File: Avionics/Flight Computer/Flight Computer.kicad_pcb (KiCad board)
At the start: 4 copper layers, 50 x 40 mm, 193 parts, among them J1 ERF8-040-05.0-S-DV-K, J2 ERF8-040-05.0-S-DV-K, J3 473460001, J4 734120110, J5 734120110, J6 734120110, U1 CC1310F128RGZR, U12 ATSAME70Q21A-AN, U2 CC1190RGVR, U3 CC2650F128RGZR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

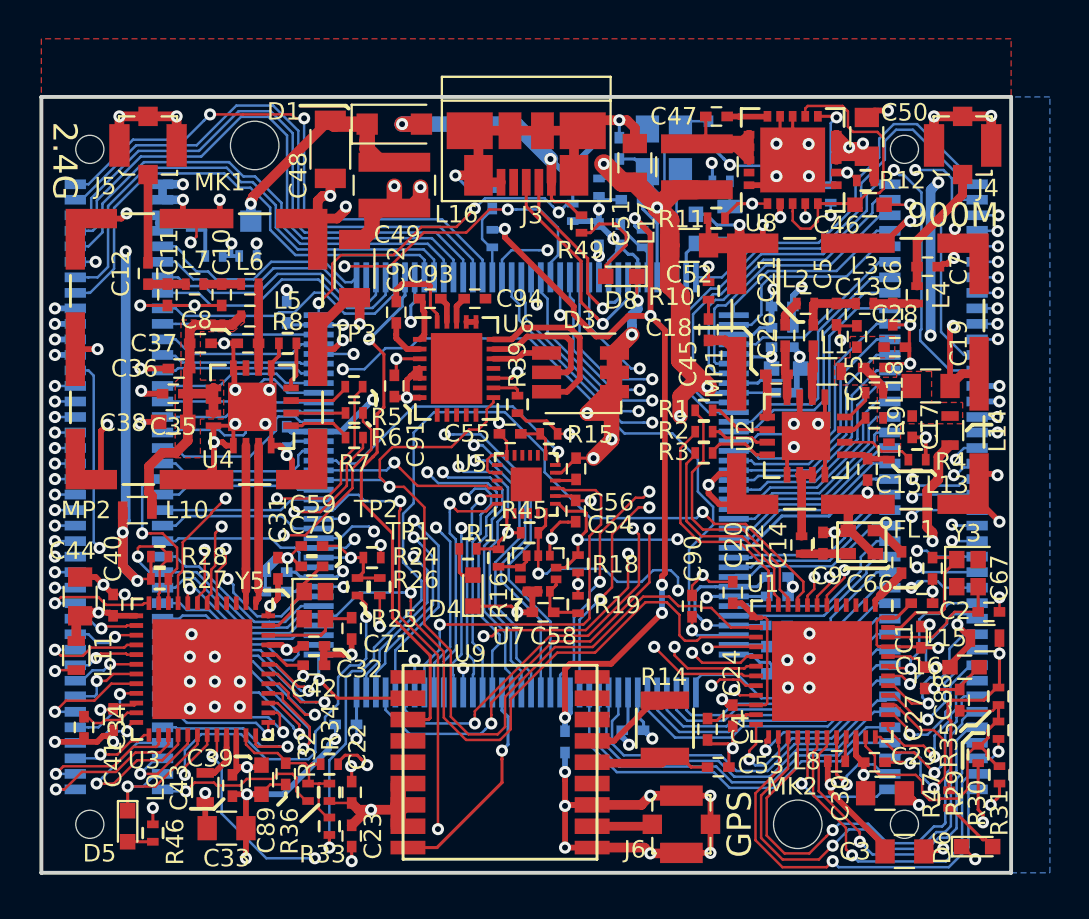
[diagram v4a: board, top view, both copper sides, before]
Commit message: Added Logo, connected GPS SDA/SCL, and cleaned silk.
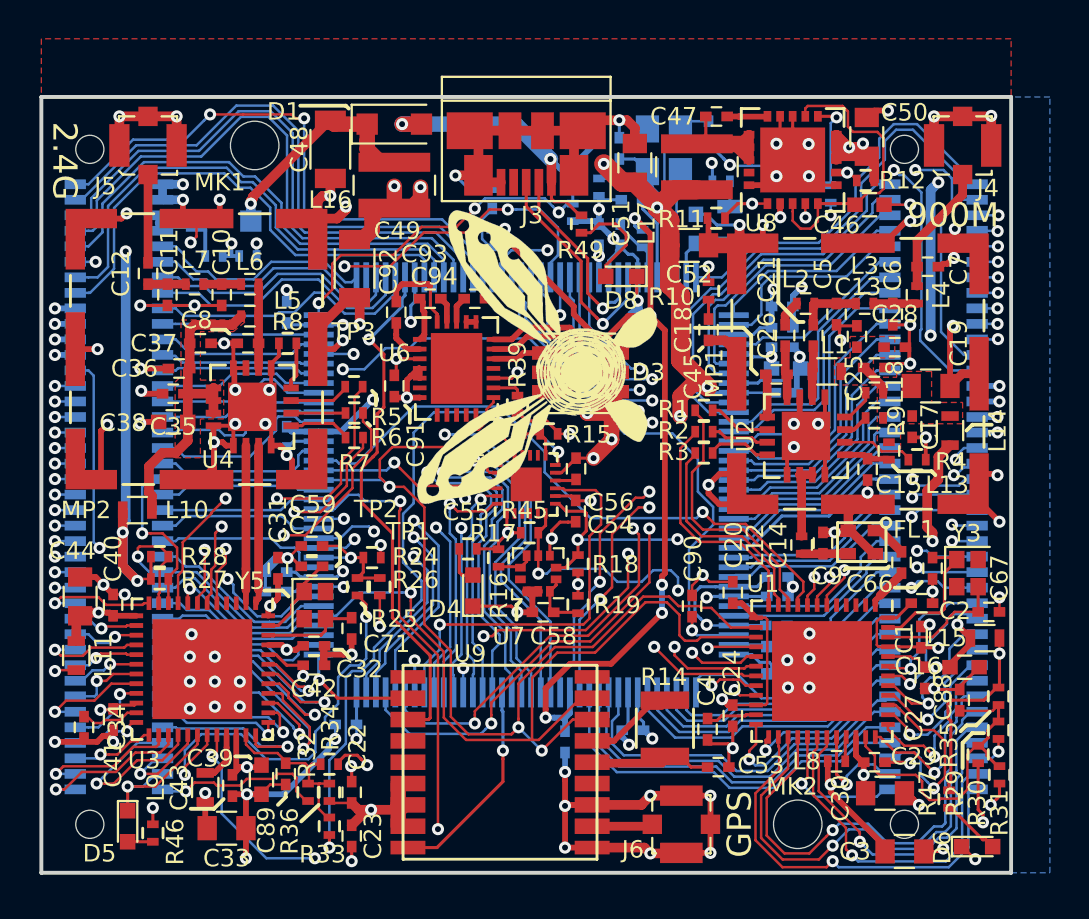
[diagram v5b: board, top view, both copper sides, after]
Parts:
- added G***: LOGO, Symbols:NaviLOGO, F.Cu at (76.2, 99.4)
- added G***: LOGO, Symbols:NaviLOGO, B.Cu at (63.2, 119.0)
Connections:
- U9 pad 16: Net-(U9-Pad16) -> /CPU-SDA
- U9 pad 17: Net-(U9-Pad17) -> /CPU-SCK
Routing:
- net /CPU-SDA: track 64.2 -> 69.6 mm, vias 2 -> 4
- net /CPU-SCK: track 66.5 -> 71.4 mm
- net Net-(C57-Pad1): track 101.4 -> 102.5 mm
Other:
- board text added: "Navi"
- board text added: "Rev 1"

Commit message: Added option resistors for IMU to be connected to radio chips via I2C
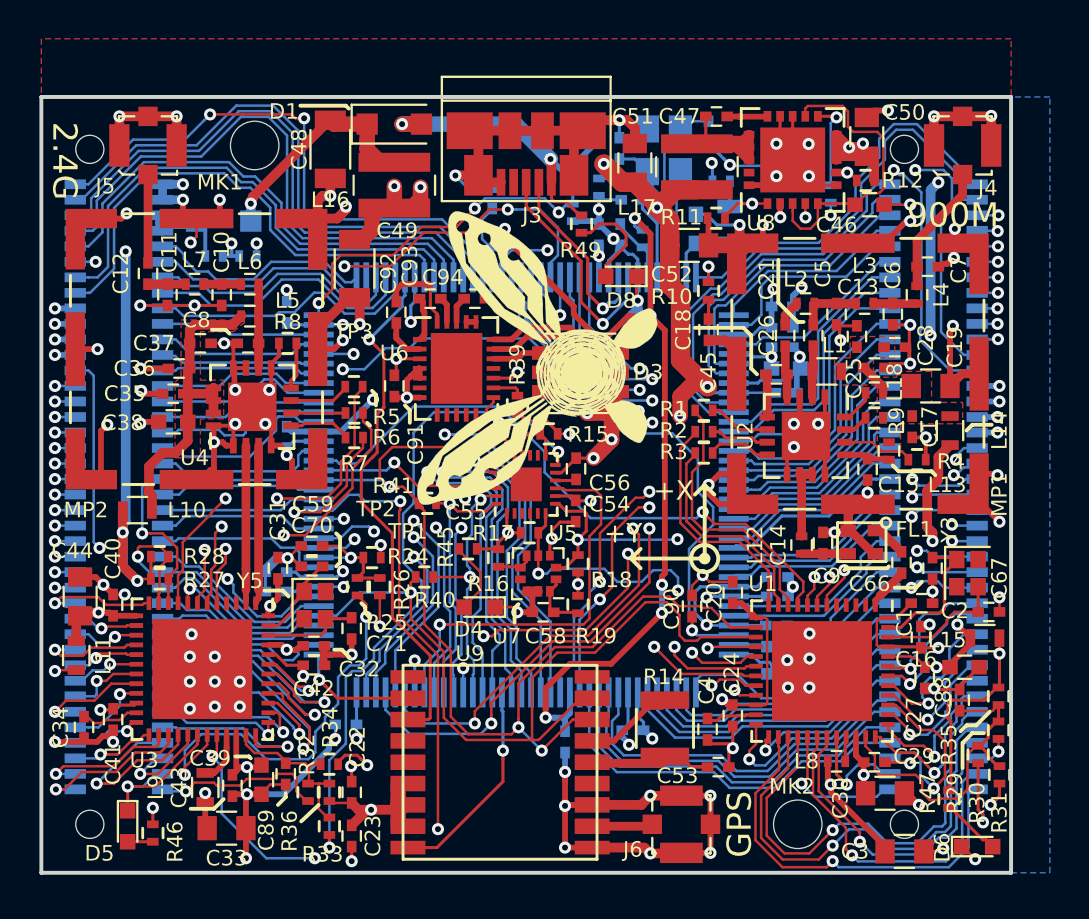
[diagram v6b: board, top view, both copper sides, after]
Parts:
- removed G*** (x2): LOGO, Symbols:NaviLOGO
- added R40: DNP, Resistors_SMD:R_0402, F.Cu at (69.8, 109.8)
- added R41: DNP, Resistors_SMD:R_0402, F.Cu at (69.9, 106.0)
- added U10: Logo, Symbols:NaviLOGO, B.Cu at (63.1, 119.0)
- added U11: Logo, Symbols:NaviLOGO, F.Cu at (76.2, 99.5)
- moved D4 0.92 mm to (72.6, 111.3), turned to 180 degrees
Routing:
- net Net-(D4-Pad2): track 1.97 -> 4.15 mm
- net /GNC_Processor/IMU-SPI-CLK: track 11.3 -> 13.4 mm, vias 1 -> 2
- net GND: track 322.9 -> 321.7 mm
- net /CPU-SCK: track 71.4 -> 72.3 mm
- net Net-(C57-Pad1): track 102.5 -> 101.7 mm
- net /GNC_Processor/IMU-SPI-MOSI: track 12.9 -> 13.6 mm
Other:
- board text added: "+X"
- board text added: "+Y"

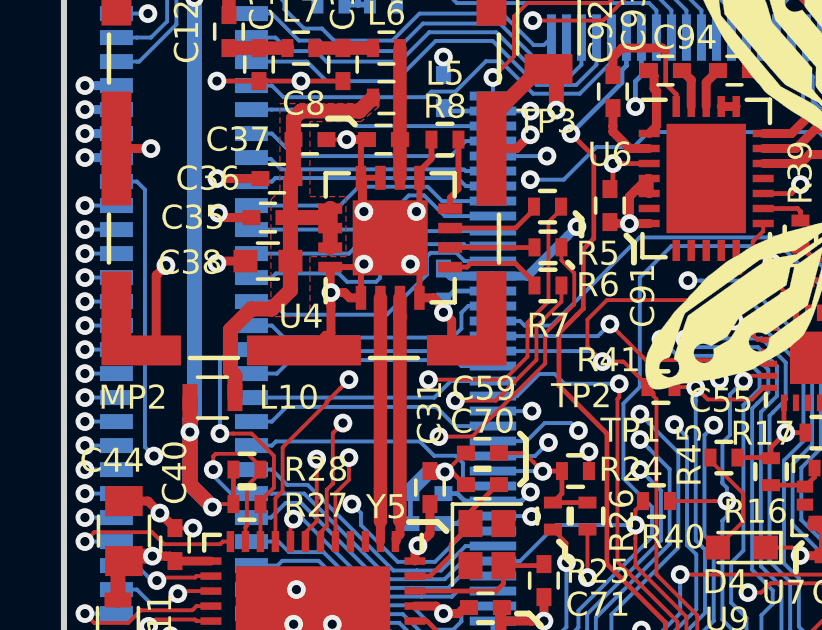
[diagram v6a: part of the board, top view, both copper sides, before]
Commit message: Added pullup to CS
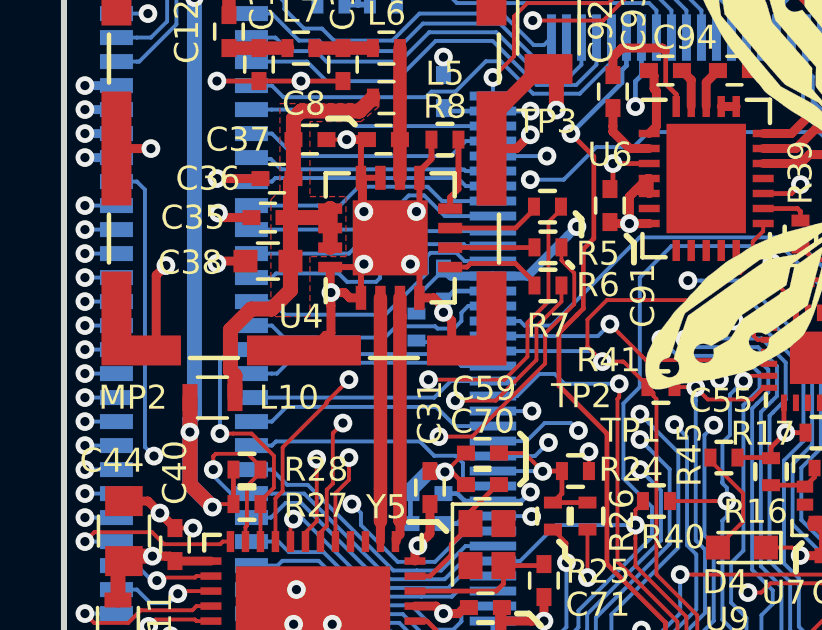
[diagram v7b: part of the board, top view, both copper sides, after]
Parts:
- added R42: 10k, Resistors_SMD:R_0402, B.Cu at (61.8, 104.0)
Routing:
- net /GNC_Processor/IMU-SPI-~CS: track 9.91 -> 12.5 mm
- net +3V3: track 138.9 -> 140.8 mm
